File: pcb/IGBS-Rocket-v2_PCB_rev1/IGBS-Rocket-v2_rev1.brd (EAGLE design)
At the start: 259.1 x 35.2 mm, 178 parts, among them Q1 BC817, Q2 ENC-03, Q3 BSS316N-H6327, U1 STM32H750VBT6, U2 LD1085D2M-R, U3 LD1085D2M-R, U4 LM317SX/NOPB, U5 MICROSD, U6 ESP-12E/F, U8 LP324DRG4, U9 MCP6V51T-E/MS, Y1 24MHz

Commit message: + PCB BOM
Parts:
- C16, C17, C26, C27, C28: device rcl2:C0603K -> rcl2:C0805K
- L1, L2, L3: device rcl2:0603 -> rcl2:0805
- R53: value 75k -> 59k

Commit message: * PCB layout 30 % T strain-gauge modules to sch
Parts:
- removed C3: 10u, SparkFun-Capacitors:0805-CAP
- removed C8: 10u Tant, rcl2:CT3216
- removed D2: GREEN, leds:LED-1206
- removed R4: 150R, rcl2:R0603
- removed R5: 560R, rcl2:R0603
- removed R6: 1K8, rcl2:R0603
- removed SRV2-A, SRV2-B: S3B-XH-A(LF)(SN)CONN_S3B-XH-A(LF)(SN)_JST, jst-XH2:CONN_S3B-XH-A(LF)(SN)_JST
- removed U3: LD1085D2M-R, ldo:D2PAK/A_STM
- added C32: 330u, rcl2:E2,5-7
- added H5, H6: MOUNT-PAD-ROUND2.8, holes:2,8-PAD
- added R60, R61: 1K, rcl2:R0603
- C1: value 100u -> 680u
- moved BTN1 248.4 mm to (148.6, 5.08)
- moved RESET 234.2 mm to (137.2, 5.08)
- moved D1 213.7 mm to (11.4, 2.54)
- moved R3 202.3 mm to (26.7, 2.54)
- moved D3 202.3 mm to (11.4, 7.62)
- moved D4 199.1 mm to (11.4, 5.08), turned to 180 degrees
- moved R1 194.4 mm to (25.4, 27.9), turned to 90 degrees
- moved C6 193.2 mm to (31.8, 21.6), turned to 180 degrees
- moved R7 191.0 mm to (26.7, 7.62)
- moved R2 187.5 mm to (27.9, 24.1), turned to 180 degrees
- moved U9 177.1 mm to (149.9, 16.5)
- moved D14 176.8 mm to (34.3, 36.8)
- moved D9 168.7 mm to (11.4, 31.8)
- moved B1 165.6 mm to (92.7, -40.6)
- moved D10 159.6 mm to (16.5, 31.8)
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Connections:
- removed net 6V-2: C8.+, R4.2, R6.2, SRV2-A.1, SRV2-B.1, U3.2, U3.4
- removed net N$11: R4.1, R5.2, U3.1
- removed net N$12: D2.A, R6.1
- removed net N$20: D15.C, R57.1
- removed net N$24: C21.1, RESET.1
- removed net N$25: C21.2, RESET.3
- removed net N$26: BTN1.1, C22.1
- removed net N$27: BTN1.3, C22.2
- removed net SRV2-A: SRV2-A.2, U1.61
- removed net SRV2-B: SRV2-B.2, U1.64
- new net BTN12: BTN1.2, R14.2, R61.1
- new net N$18: C1.+, C2.1, D7.C, MOV1.1, PPTC1.2, U2.3
- new net NRST2: R29.2, R60.1, RESET.2
- net ANG-RATE: now also D15.C, R57.1
- net BAT: no longer C1.+, C2.1, C3.1, D7.C, MOV1.1, PPTC1.2, U2.3, U3.3
- net BTN1: now also C22.1, R61.2; no longer BTN1.2, R14.2
- net GND: now also C21.2, C22.2, C32.-, H5.B2,8, H6.B2,8; no longer C3.2, C8.-, D2.C, R5.1, SRV2-A.3, SRV2-B.3
- net N$39: now also C32.+
- net NRST: now also C21.1, R60.2; no longer R29.2, RESET.2
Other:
- board size 259.1 x 35.2 mm -> 199.4 x 35.2 mm

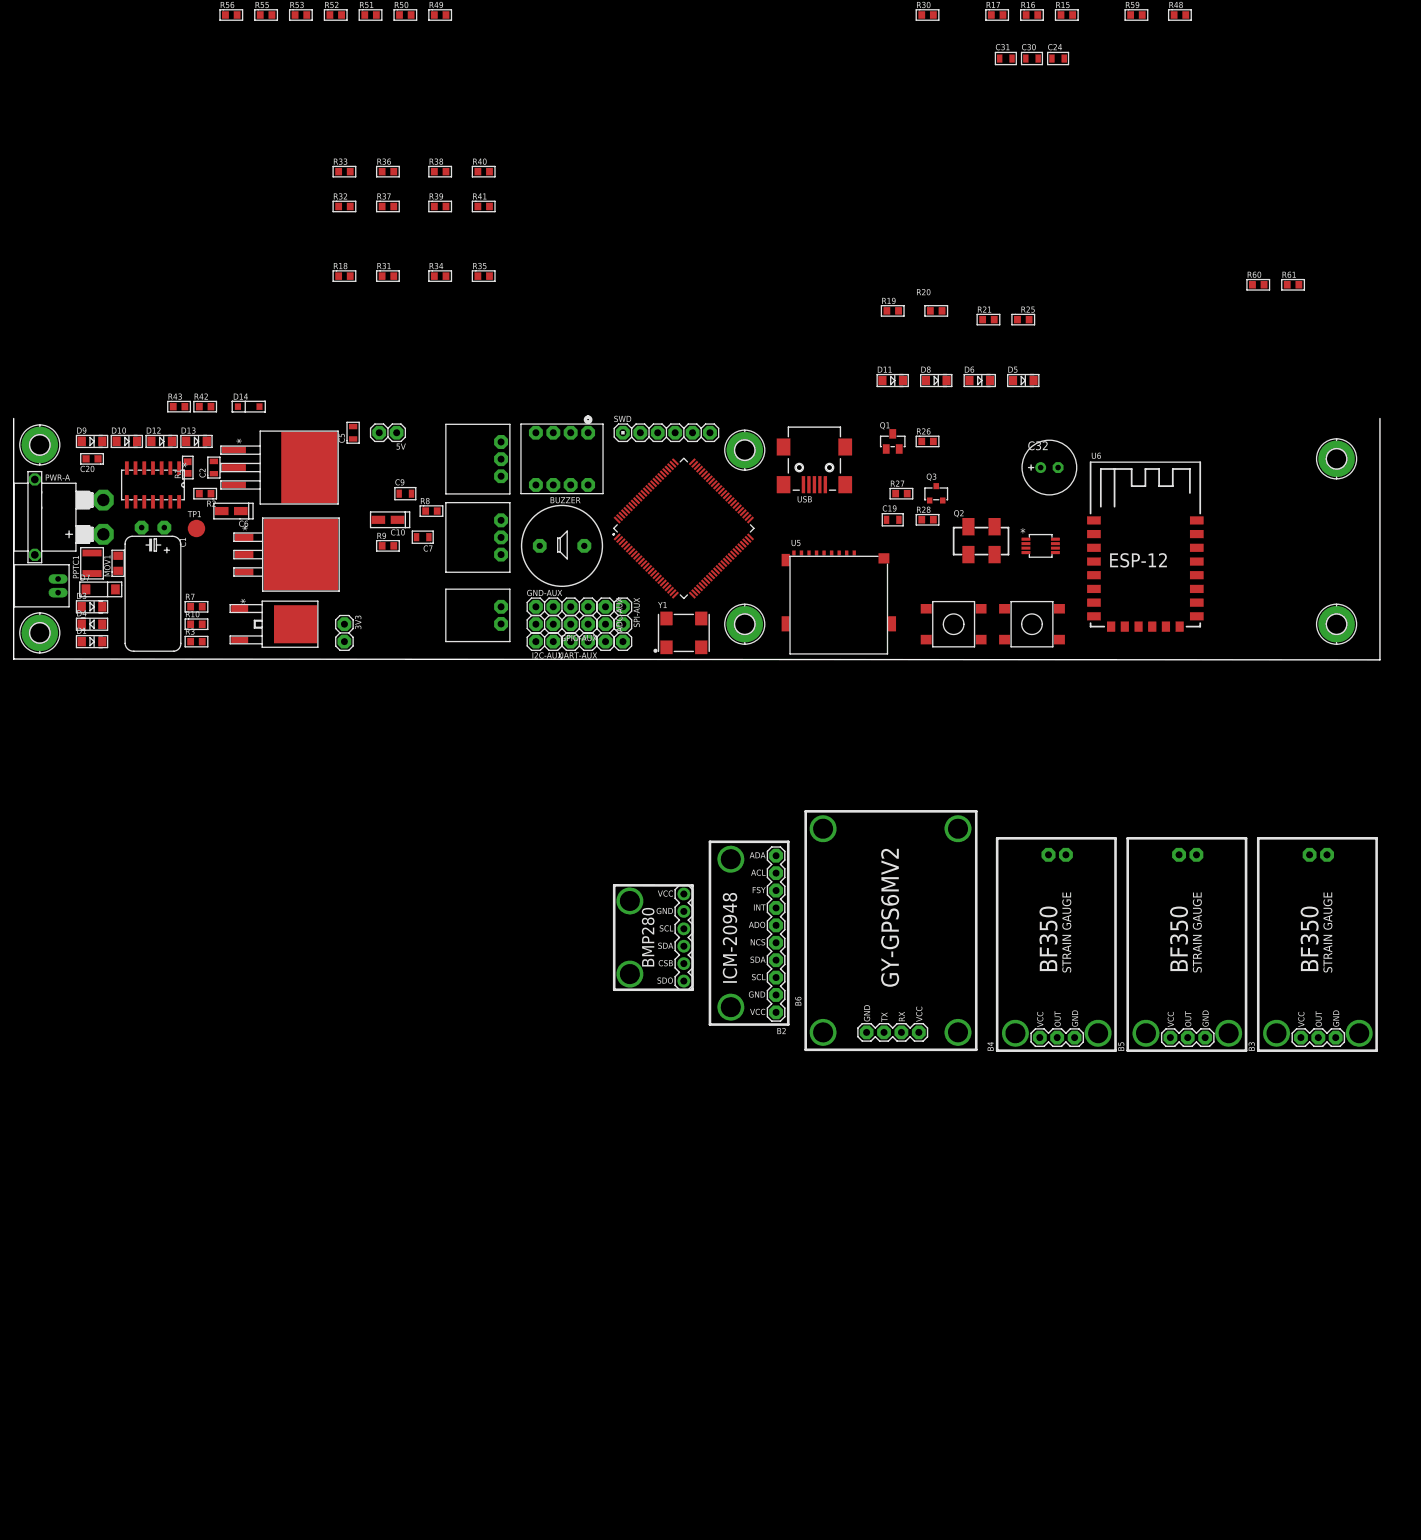
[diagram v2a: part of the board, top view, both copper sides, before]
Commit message: + PCB schematic is DONE + BOM (Mouser) is DONE
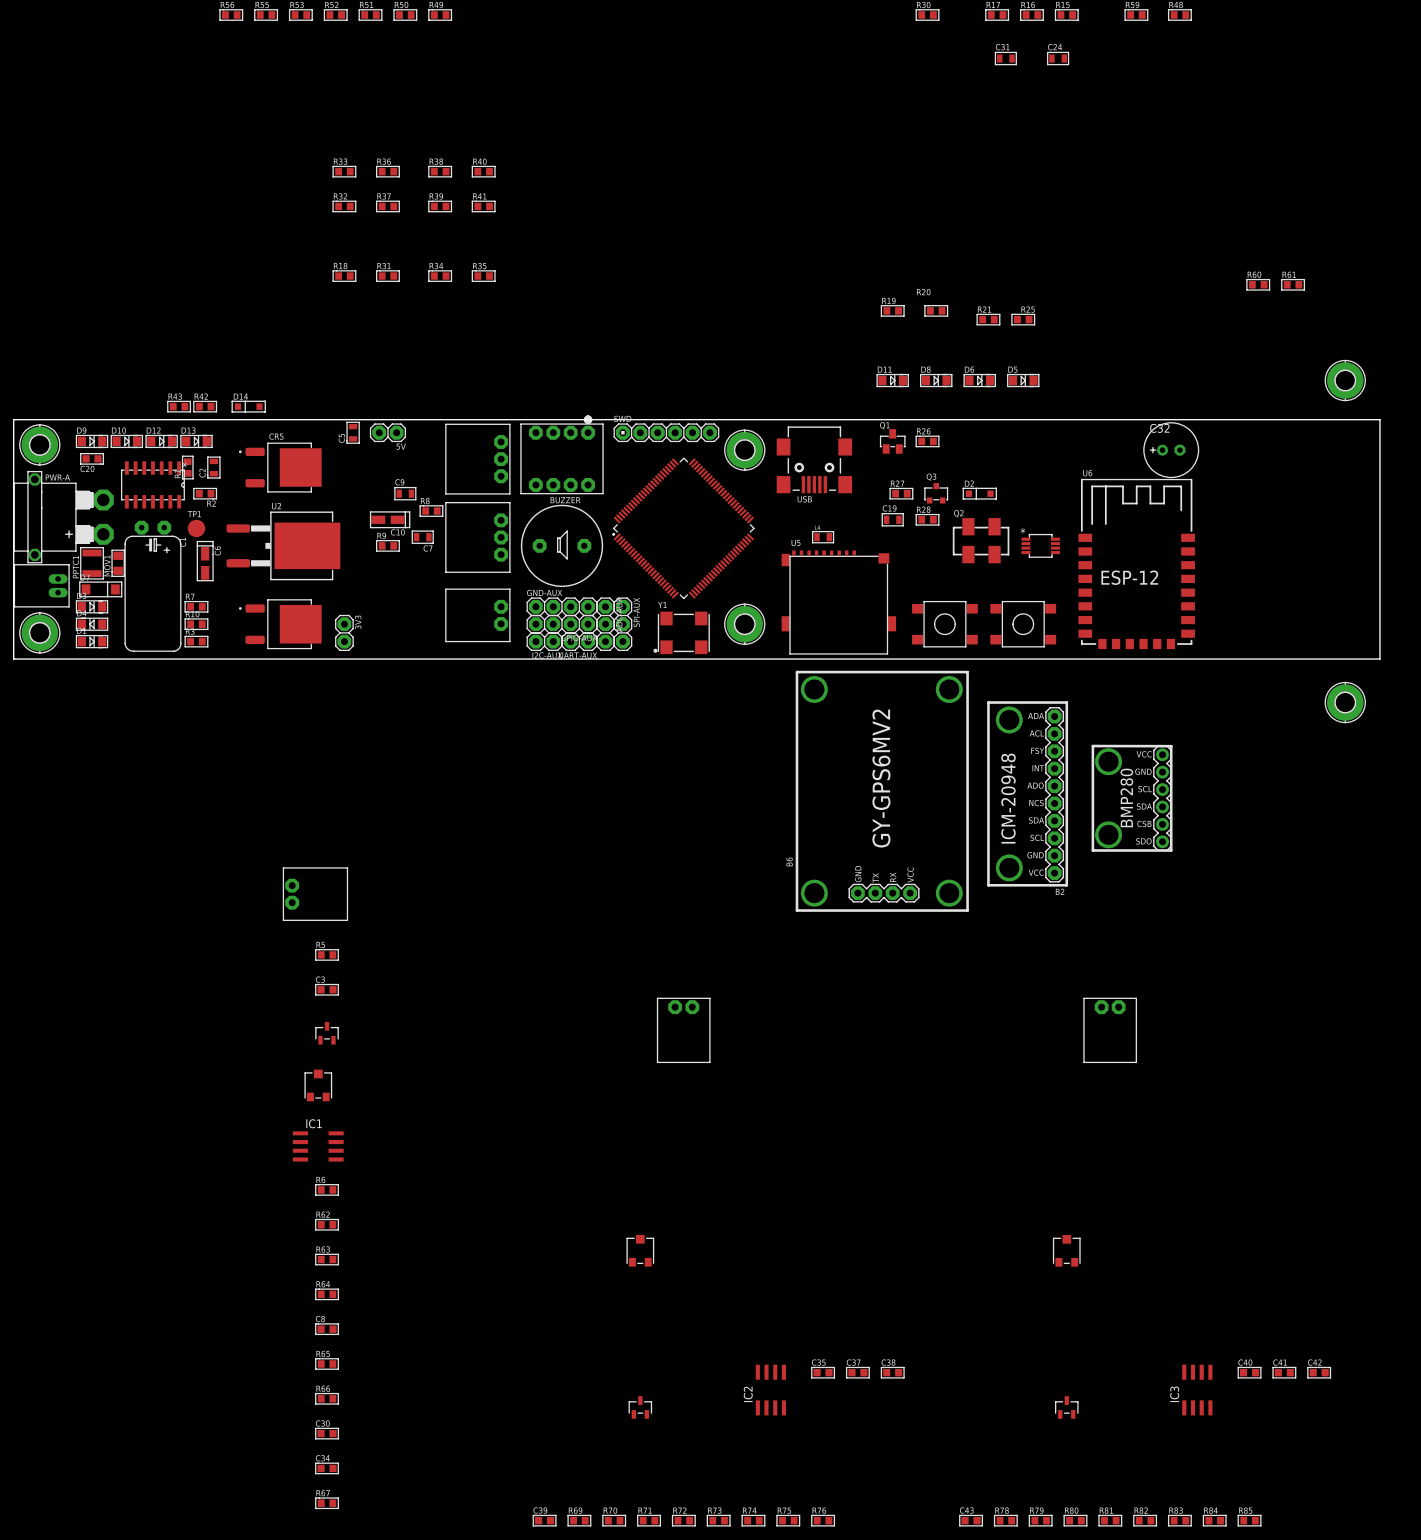
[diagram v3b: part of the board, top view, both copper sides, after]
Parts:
- removed B3, B4, B5: BF350, modules:BF350
- removed U4: LM317SX/NOPB, linreg:TS3B_TEX
- added C3, C35, C40: 100n, rcl2:C0603K
- added C34, C37, C38, C39, C41, C42, C43, C8: 1u, rcl2:C0603K
- added CR2, CR3, CR4: TS4040DILT-2.5, ref:SOT23_TO-236AB_NEX
- added CR5: AZ2185D, ldo:DPAK229P990X239-3N
- added D2: 3V6, SparkFun-DiscreteSemi:SOD-123
- added IC1, IC2, IC3: NCV21872DR2G, opamps:SO08
- added L4: 10uH, rcl2:0805
- added R4, R68, R77: 500k, trimmer:RES_C01R00
- added R5, R69, R78: 10k, rcl2:R0603
- added R6, R62, R63, R70, R71, R72, R79, R80, R81: 360R, rcl2:R0603
- added R64, R66, R73, R75, R82, R84: 470k, rcl2:R0603
- added R65, R74, R83: 20k, rcl2:R0603
- added R67, R76, R85: 330R, rcl2:R0603
- added SG1, SG2, SG3: S3B-XH-A, jst-XH2:CONN_S2B-XH-A_JST
- C30: value 10u -> 1u; device SparkFun-Capacitors:0805-CAP -> rcl2:C0603K
- CR1: device ldo:DPAK_STM -> ldo:DPAK229P990X239-3N
- U2: value LD1085D2M-R -> LM317BD2TG; device ldo:D2PAK/A_STM -> linreg:TO263
- moved C30 225.5 mm to (45.7, -113.0)
- moved B1 72.7 mm to (162.6, -20.3)
- moved B2 45.4 mm to (147.3, -20.3)
- moved H1 35.6 mm to (194.3, 40.6)
- moved H2 35.6 mm to (194.3, -6.35)
- moved B6 20.4 mm to (127.0, -26.5)
- moved C32 18.0 mm to (168.9, 30.5)
- moved U2 11.5 mm to (39.4, 16.5)
- moved C6 8.52 mm to (27.9, 14.0), turned to 270 degrees
- moved U6 2.84 mm to (163.8, 10.2)
- moved BTN1 1.27 mm to (147.3, 5.08)
- moved RESET 1.27 mm to (135.9, 5.08)
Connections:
- removed net GAUG1: B3.2, TP16.TP, U1.33
- removed net GAUG2: B4.2, TP17.TP, U1.34
- removed net GAUG3: B5.2, TP18.TP, U1.35
- new net ANG-RATE2: C28.2, R53.1, R57.2, U9.6
- new net N$11: R5.2, R6.1, SG1.1
- new net N$12: C8.2, IC1.3, R62.1, R63.2
- new net N$20: R69.2, R70.1, SG2.1
- new net N$24: IC1.2, R5.1, R64.2
- new net N$25: IC1.1, R64.1, R65.2
- new net N$26: IC1.6, R65.1, R66.2
- new net N$53: C34.2, IC1.5, R4.2
- new net N$54: CR2.1, R4.1, R63.1, R67.1, SG1.2
- new net N$55: C37.2, IC2.3, R71.1, R72.2
- new net N$56: IC2.2, R69.1, R73.2
- new net N$57: IC2.1, R73.1, R74.2
- new net N$58: IC2.6, R74.1, R75.2
- new net N$60: C39.2, IC2.5, R68.2
- new net N$61: CR3.1, R68.1, R72.1, R76.1, SG2.2
- new net N$62: R78.2, R79.1, SG3.1
- new net N$63: C41.2, IC3.3, R80.1, R81.2
- new net N$64: IC3.2, R78.1, R82.2
- new net N$65: IC3.1, R82.1, R83.2
- new net N$66: IC3.6, R83.1, R84.2
- new net N$68: C43.2, IC3.5, R77.2
- new net N$69: CR4.1, R77.1, R81.1, R85.1, SG3.2
- new net SG1: C30.2, IC1.7, R66.1, TP16.TP, U1.33
- new net SG2: C38.2, IC2.7, R75.1, TP17.TP, U1.34
- new net SG3: C42.2, IC3.7, R84.1, TP18.TP, U1.35
- net 3V3: now also D2.C, L4.2, U2.2; no longer R44.2, R45.2, R46.2, R47.2, U4.2, U4.4
- net 5V: now also C3.2, C35.2, C40.2, CR1.2, IC1.8, IC2.8, IC3.8, R67.2, R76.2, R85.2; no longer B3.1, B4.1, B5.1, CR1.3
- net 6V-1: now also CR5.2; no longer U2.2, U2.4
- net ANG-RATE: now also D2.A; no longer C28.2, R53.1, R57.2, U9.6
- net BAT: now also CR1.3, U2.3; no longer CR1.2, U4.3
- net GND: now also C3.1, C30.1, C34.1, C35.1, C37.1, C38.1, C39.1, C40.1, C41.1, C42.1, C43.1, C8.1, CR2.2, CR2.3, CR3.2, CR3.3, CR4.2, CR4.3, IC1.4, IC2.4, IC3.4, R4.3, R6.2, R62.2, R68.3, R70.2, R71.2, R77.3, R79.2, R80.2; no longer B3.3, B3.HOLE1, B3.HOLE2, B4.3, B4.HOLE1, B4.HOLE2, B5.3, B5.HOLE1, B5.HOLE2, C30.2
- net N$15: now also U2.1; no longer U4.1
- net N$18: now also CR5.3; no longer U2.3
- net N$39: no longer C30.1
- net N$9: now also CR5.1; no longer U2.1
- net VCC: now also L4.1, R44.2, R45.2, R46.2, R47.2
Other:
- board size 199.4 x 35.2 mm -> 199.4 x 34.9 mm

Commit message: * PCB: 12V regulator added, P-FET HSS is now last missing part
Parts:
- removed 3V3, 5V: (no value), pinhead2:1X02
- removed SRV1-A: S3B-XH-A, jst-XH2:CONN_S3B-XH-A(LF)(SN)_JST
- removed SRV1-B: S3B-XH-A(LF)(SN)CONN_S3B-XH-A(LF)(SN)_JST, jst-XH2:CONN_S3B-XH-A(LF)(SN)_JST
- added 12V-AUX, 3V3-AUX, 5V-AUX: (no value), pinhead2:1X02
- added 12V-CAM: S2B-XH-A(LF)(SN)CONN_S2B-XH-A_JST, jst-XH2:CONN_S2B-XH-A_JST
- added C44, C46: 22u, SparkFun-Capacitors:0805-CAP
- added C45: 100n, rcl2:C0805K
- added C47: 10n, rcl2:C0805K
- added CR6: SS12, diode2:DIODE_DO214AC
- added D17: GREEN, leds:LED-1206
- added L5: 22u, rcl2:IND_74437_WRE
- added R86: 3K6, rcl2:R0603
- added R87: 4.87k, rcl2:R0603
- added R88: 1.27k, rcl2:R0603
- added R89, R90: 5k, rcl2:R0603
- added R91: 8k1, rcl2:R0603
- added R92, R93, R95: 10k, rcl2:R0603
- added R94: 30k, rcl2:R0603
- added R96: 1K, rcl2:R0603
- added R97: 22R, rcl2:R0603
- added SRV1: S3B-XH-A, jst-XH2:CONN_S3B-XH-A(LF)(SN)_JST
- added SRV2, SRV3: S3B-XH-A(LF)(SN)CONN_S3B-XH-A(LF)(SN)_JST, jst-XH2:CONN_S3B-XH-A(LF)(SN)_JST
- added TP22, TP23, TP24: TPB1,27, testpad2:B1,27
- added U$1: SHORT, testpad2:SHORT
- added U3: CS5171EDR8G, dc-dc:SOIC8_ONS
- GND-AUX: device pinhead2:1X04 -> pinhead2:1X02
- PPTC1: value 6V/2A -> 10V/8A
- moved IC1 162.3 mm to (174.0, 26.7)
- moved SG1 153.6 mm to (181.6, 25.4)
- moved R4 151.9 mm to (167.6, 26.7)
- moved CR3 145.6 mm to (162.6, 17.8)
- moved CR2 142.3 mm to (162.6, 26.7)
- moved IC2 139.7 mm to (174.0, 17.8), turned to 270 degrees
- moved R68 129.0 mm to (167.6, 17.8)
- moved CR4 118.4 mm to (162.6, 8.89)
- moved IC3 115.6 mm to (174.0, 8.89), turned to 270 degrees
- moved SG2 108.5 mm to (181.6, 16.5), turned to 90 degrees
- moved R77 96.3 mm to (167.6, 8.89)
- moved BTN1 81.4 mm to (66.0, 10.2)
- moved R40 71.1 mm to (16.4, 22.9), flipped to the bottom, turned to 270 degrees
- moved RESET 71.0 mm to (66.0, 17.8)
- moved R41 65.4 mm to (16.4, 26.7), flipped to the bottom, turned to 270 degrees
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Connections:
- removed net 6V-1: C6.+, CR5.2, R1.2, R3.2, SRV1-A.1, SRV1-B.1
- removed net SRV1-A: SRV1-A.2, U1.22
- removed net SRV1-B: SRV1-B.2, U1.23
- new net 12V: 12V-AUX.1, 12V-CAM.1, R86.2, R94.2
- new net 12V-SCALED: R94.1, R95.2
- new net 5V-SCALED: R90.1, R91.2
- new net 6V: C6.+, CR5.2, R1.2, R3.2, R92.2, SRV1.1, SRV2.1, SRV3.1
- new net 6V-SCALED: R92.1, R93.2
- new net AGND: C20.1, C25.1, C27.2, C29.1, C3.1, C30.1, C34.1, C35.1, C37.1, C38.1, C39.1, C40.1, C41.1, C42.1, C43.1, C8.1, CR2.2, CR2.3, CR3.2, CR3.3, CR4.2, CR4.3, D15.A, IC1.4, IC2.4, IC3.4, Q2.2, R4.3, R6.2, R62.2, R68.3, R70.2, R71.2, R77.3, R79.2, R80.2, U$1.AGND, U1.19, U3.6, U8.11, U9.4
- new net N$27: CR6.2, L5.1, U3.8
- new net N$59: D17.A, R86.1
- new net N$67: C46.1, CR6.1, R87.2
- new net N$70: C47.2, R89.1
- new net N$71: R89.2, U3.1
- new net SRV1: SRV1.2, TP22.TP, U1.22
- new net SRV2: SRV2.2, TP23.TP, U1.23
- new net SRV3: SRV3.2, TP24.TP, U1.61
- net 3V3: now also 3V3-AUX.1; no longer 3V3.1
- net 5V: now also 5V-AUX.1, R90.2; no longer 5V.1
- net BAT: now also C1.+, C2.1, C44.1, C45.2, CR5.3, D7.C, L5.2, MOV1.1, PPTC1.2, U3.5
- net GND: now also 12V-AUX.2, 12V-CAM.2, 3V3-AUX.2, 5V-AUX.2, C44.2, C45.1, C46.2, C47.1, D17.C, R88.1, R91.1, R93.1, R95.1, SRV1.3, SRV2.3, SRV3.3, U$1.GND, U3.7; no longer 3V3.2, 5V.2, C20.1, C25.1, C27.2, C29.1, C3.1, C30.1, C34.1, C35.1, C37.1, C38.1, C39.1, C40.1, C41.1, C42.1, C43.1, C8.1, CR2.2, CR2.3, CR3.2, CR3.3, CR4.2, CR4.3, D15.A, GND-AUX.3, GND-AUX.4, IC1.4, IC2.4, IC3.4, Q2.2, R4.3, R6.2, R62.2, R68.3, R70.2, R71.2, R77.3, R79.2, R80.2, SRV1-A.3, SRV1-B.3, U1.19, U8.11, U9.4
- net N$18: now also R87.1, R88.2, U3.2; no longer C1.+, C2.1, CR5.3, D7.C, MOV1.1, PPTC1.2

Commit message: + PCB schematics is DONE (added 12V BOOST + 3 servos)
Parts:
- added Q4: BC817, transistor-npn:SOT23-BEC
- added Q5: BSS314PE, SparkFun-DiscreteSemi:SOT23-3
- added R98: 10K, rcl2:R0603
- added TP25: TPB1,27, testpad2:B1,27
- Q3: value BSS316N-H6327 -> BSS316N
- R90: value 5k -> 4k7
- R91: value 8k1 -> 7k5
- R97: value 22R -> 4k7
- moved R96 17.8 mm to (-31.8, -325.1)
- moved Q1 2.84 mm to (110.5, 32.0)
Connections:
- net N$2 renamed BAT2
- new net 12V-HOT: C46.1, CR6.1, Q5.2, R87.2, R97.1
- new net CTRL-12V: R96.2, TP25.TP, U1.7
- new net N$72: Q4.C, Q5.1, R97.2
- net 12V: now also Q5.3
- net 12V-SCALED: now also U1.25
- net 5V-SCALED: now also U1.24
- net 6V-SCALED: now also U1.16
- net ESP-RX: now also U1.86; no longer U1.24
- net ESP-TX: now also U1.87; no longer U1.25
- net GND: now also Q4.E, R98.1
- net GPS-TX: now also U1.69; no longer U1.54
- net ICM-MOSI: now also U1.54; no longer U1.16
- net N$67: now also Q4.B, R96.1, R98.2; no longer C46.1, CR6.1, R87.2

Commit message: + PCB layout done (DXF, STEP, BRD, PNG)
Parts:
- removed 12V-AUX: (no value), pinhead2:1X02
- removed TP16, TP17, TP18: TPB1,27, testpad2:B1,27
- added TP26, TP27, TP28: TPB1,27, testpad2:B1,27
- B1: device modules:BMP280 -> modules:BMP280-LESSPINS
- B2: device modules:ICM-20948 -> modules:ICM-20948-LESSPINS
- H1, H2, H3, H4, H5, H6: device holes:2,8-PAD -> holes3:2,8-PAD
- moved TP25 343.5 mm to (22.9, 2.54), flipped to the bottom
- moved Q5 342.8 mm to (31.4, 6.48), flipped to the bottom, turned to 90 degrees
- moved R98 338.1 mm to (27.9, 2.54), flipped to the bottom, turned to 270 degrees
- moved R96 332.6 mm to (25.4, 2.54), flipped to the bottom, turned to 270 degrees
- moved Q4 327.5 mm to (31.8, 2.54), flipped to the bottom, turned to 90 degrees
- moved R97 323.6 mm to (33.4, 4.57), flipped to the bottom
- moved R93 323.2 mm to (40.6, 22.9), flipped to the bottom, turned to 180 degrees
- moved R95 321.7 mm to (27.9, 13.8), flipped to the bottom, turned to 270 degrees
- moved R92 320.7 mm to (40.6, 25.4), flipped to the bottom
- moved R94 313.0 mm to (27.9, 10.1), flipped to the bottom, turned to 270 degrees
- moved R91 297.8 mm to (51.1, 4.15), flipped to the bottom, turned to 270 degrees
- moved R90 292.4 mm to (49.1, 4.13), flipped to the bottom, turned to 90 degrees
- moved U$1 284.8 mm to (3.81, 10.2), turned to 90 degrees
- moved CR6 269.1 mm to (22.9, 7.62), flipped to the bottom, turned to 90 degrees
- moved 12V-CAM 245.2 mm to (31.0, 13.7), flipped to the bottom, turned to 270 degrees
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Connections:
- removed net ACL: B2.9
- removed net ADA: B2.10
- removed net CSB: B1.2
- removed net FSY: B2.8
- removed net INT: B2.7
- removed net SDO: B1.1
- new net 3V3-SD: C31.1, C36.1, L4.2, U5.4
- net 12V: no longer 12V-AUX.1
- net 3V3: no longer C31.1, C36.1, L4.2, U5.4
- net GND: no longer 12V-AUX.2
- net SG1: now also TP26.TP; no longer TP16.TP
- net SG2: now also TP27.TP; no longer TP17.TP
- net SG3: now also TP28.TP; no longer TP18.TP
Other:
- board size 199.4 x 34.9 mm -> 182.9 x 34.9 mm
- board text added: "IGBS ROCKET TEAM"
- board text added: "ITSGOODBUTSILL.COM"
- board text added: "rev1 23-03-22 JP"
